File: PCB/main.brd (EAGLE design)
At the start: 100 x 100 mm, 81 parts, among them X1 BU-SMA-V

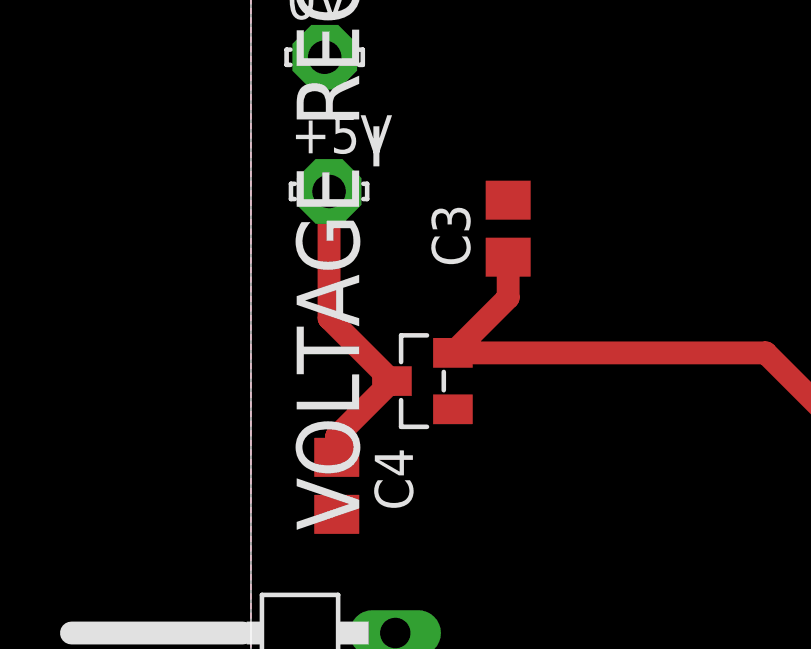
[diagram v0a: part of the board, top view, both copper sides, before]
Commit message: PCB Schematic Change
5V Supply Pad was not connected to 5V net
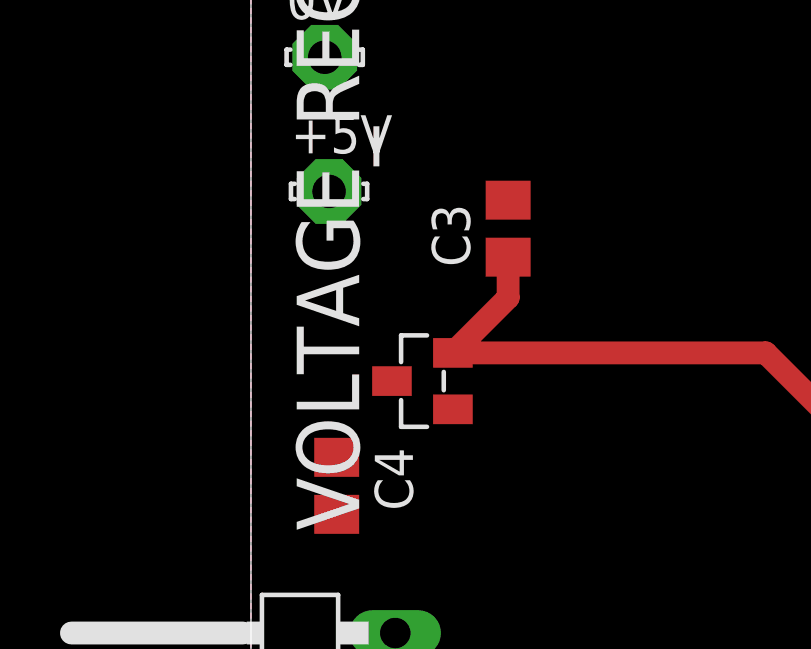
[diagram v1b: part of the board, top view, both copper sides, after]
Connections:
- removed net N$2: +5V.MP, C4.1, VOLTAGE_REGULATOR.3
- net +5V: now also +5V.MP, C4.1, VOLTAGE_REGULATOR.3
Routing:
- net N$2: track 10.5 -> 0.00 mm
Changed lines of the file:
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@@
 <wire x1="75.438" y1="73.152" x2="78.486" y2="76.2" width="0.3048" layer="1"/>
 <wire x1="78.486" y1="76.2" x2="80.4857" y2="76.2" width="0.3048" layer="1"/>
+<contactref element="C4" pad="1"/>
+<contactref element="+5V" pad="MP"/>
+<contactref element="VOLTAGE_REGULATOR" pad="3"/>
 <wire x1="31.75" y1="55.5625" x2="51.8175" y2="73.2325" width="0" layer="19" extent="1-1"/>
 <wire x1="29.21" y1="55.5625" x2="31.75" y2="55.5625" width="0" layer="19" extent="1-1"/>
 <wire x1="26.67" y1="55.5625" x2="29.21" y2="55.5625" width="0" layer="19" extent="1-1"/>
+<wire x1="4.699" y1="50.8" x2="26.67" y2="55.5625" width="0" layer="19" extent="1-1"/>
+<wire x1="2.8575" y1="48.2575" x2="4.699" y2="50.8" width="0" layer="19" extent="1-1"/>
+<wire x1="2.6025" y1="57.122" x2="4.699" y2="50.8" width="0" layer="19" extent="1-1"/>
 </signal>
 <signal name="BT-L">
@@
 <wire x1="49.2125" y1="68.3975" x2="49.3775" y2="68.2325" width="0.3048" layer="1"/>
 </signal>
-<signal name="N$2">
-<contactref element="VOLTAGE_REGULATOR" pad="3"/>
-<contactref element="C4" pad="1"/>
-<contactref element="+5V" pad="MP"/>
-<wire x1="4.699" y1="50.8" x2="2.6025" y2="52.8965" width="0.762" layer="1"/>
-<wire x1="2.6025" y1="52.8965" x2="2.6025" y2="57.122" width="0.762" layer="1"/>
-<wire x1="4.699" y1="50.8" x2="2.8575" y2="48.9585" width="0.762" layer="1"/>
-<wire x1="2.8575" y1="48.9585" x2="2.8575" y2="48.2575" width="0.762" layer="1"/>
-</signal>
 <signal name="N$10">

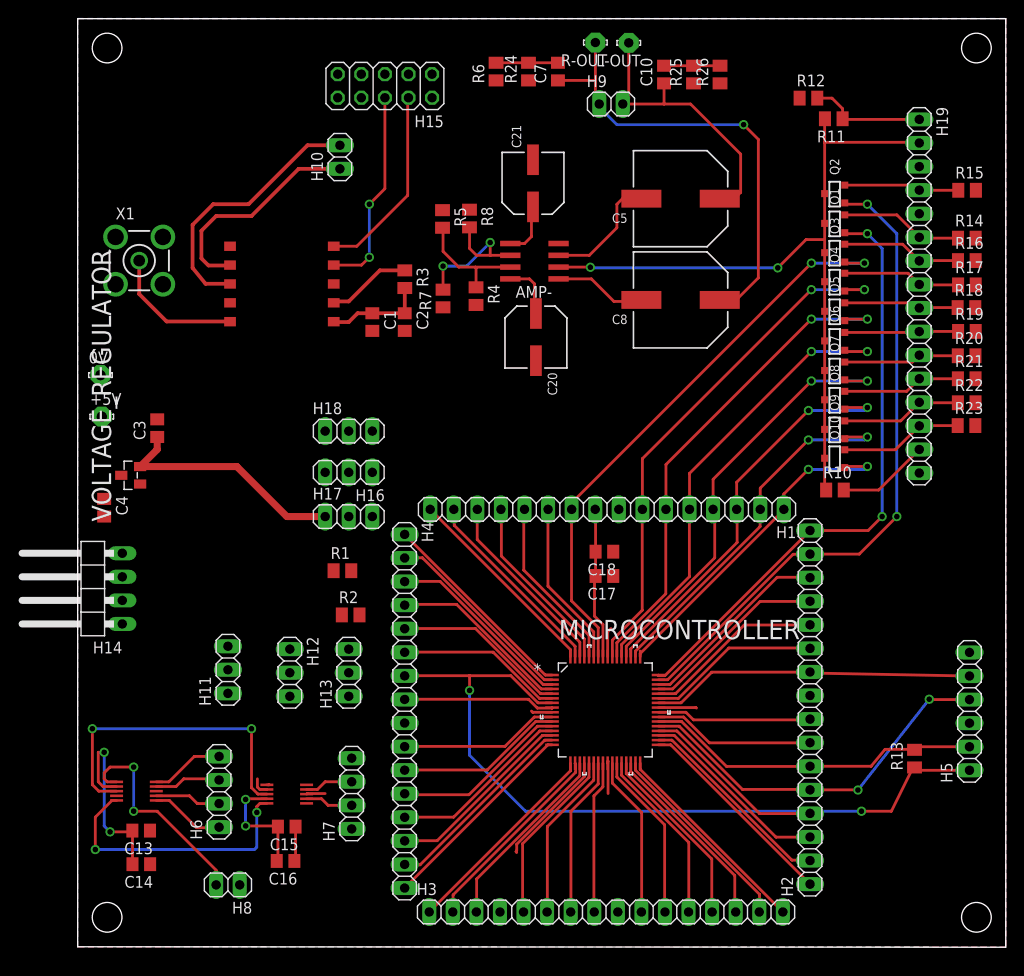
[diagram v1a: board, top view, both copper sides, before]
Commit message: PCB Layout
-All connections should be complete
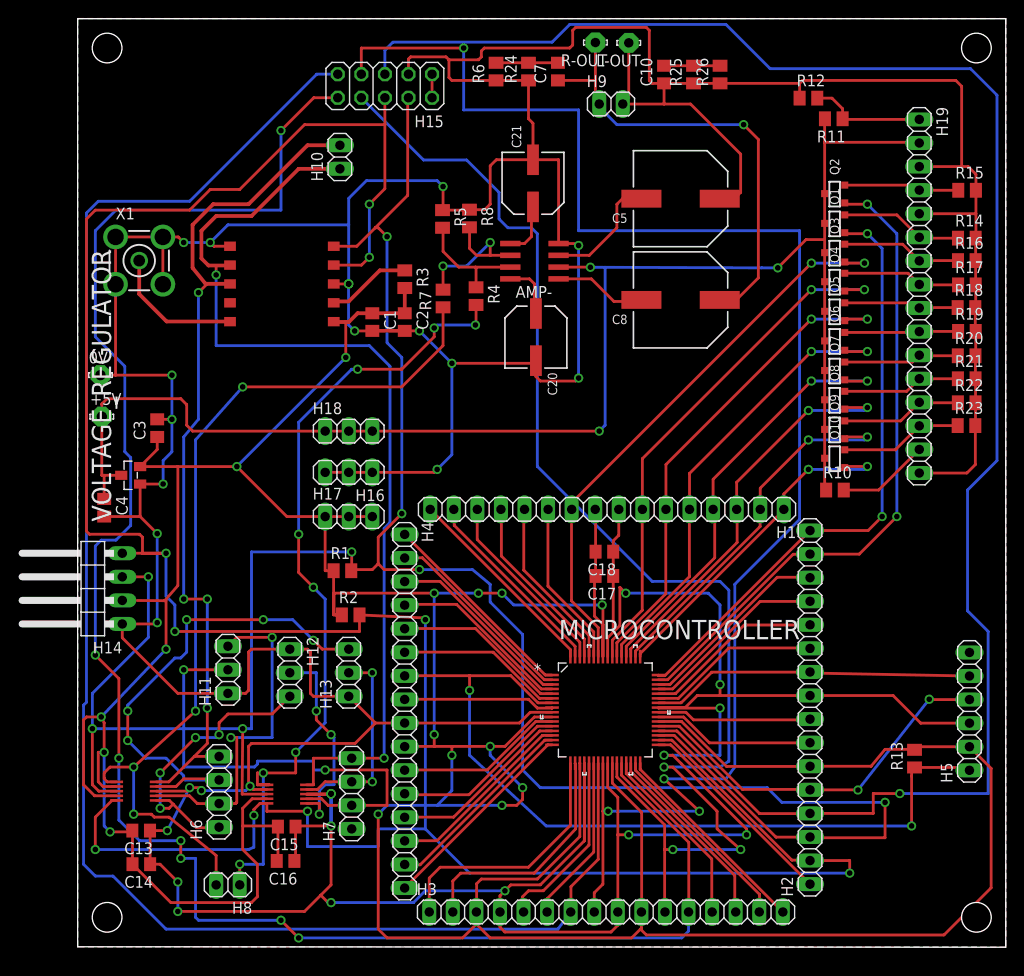
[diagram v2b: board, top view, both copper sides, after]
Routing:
- net GND: track 33.8 -> 734.7 mm, vias 0 -> 33
- net +3V3: track 179.1 -> 484.9 mm, vias 4 -> 16
- net SCL: track 73.4 -> 295.6 mm, vias 4 -> 9
- net SDA/MISO: track 76.0 -> 259.7 mm, vias 2 -> 8
- net XDCS: track 19.0 -> 198.6 mm, vias 0 -> 7
- net MOSI: track 20.0 -> 191.7 mm, vias 0 -> 1
- net XCS: track 17.3 -> 177.1 mm
- net DREQ: track 16.4 -> 170.7 mm, vias 0 -> 4
- net XRST: track 18.2 -> 142.9 mm, vias 0 -> 3
- net AMP-R: track 0.26 -> 89.0 mm, vias 0 -> 8
- net +5V: track 81.1 -> 167.8 mm, vias 2 -> 3
- net FM-R: track 24.1 -> 107.5 mm, vias 0 -> 2
- net AMP-L: track 23.4 -> 97.7 mm, vias 2 -> 4
- net FM-L: track 36.8 -> 94.3 mm, vias 0 -> 4
- net REC-L: track 7.16 -> 53.7 mm, vias 0 -> 5
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
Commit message: PCB Layout
- DRC performed (all clearance settings 6mil)
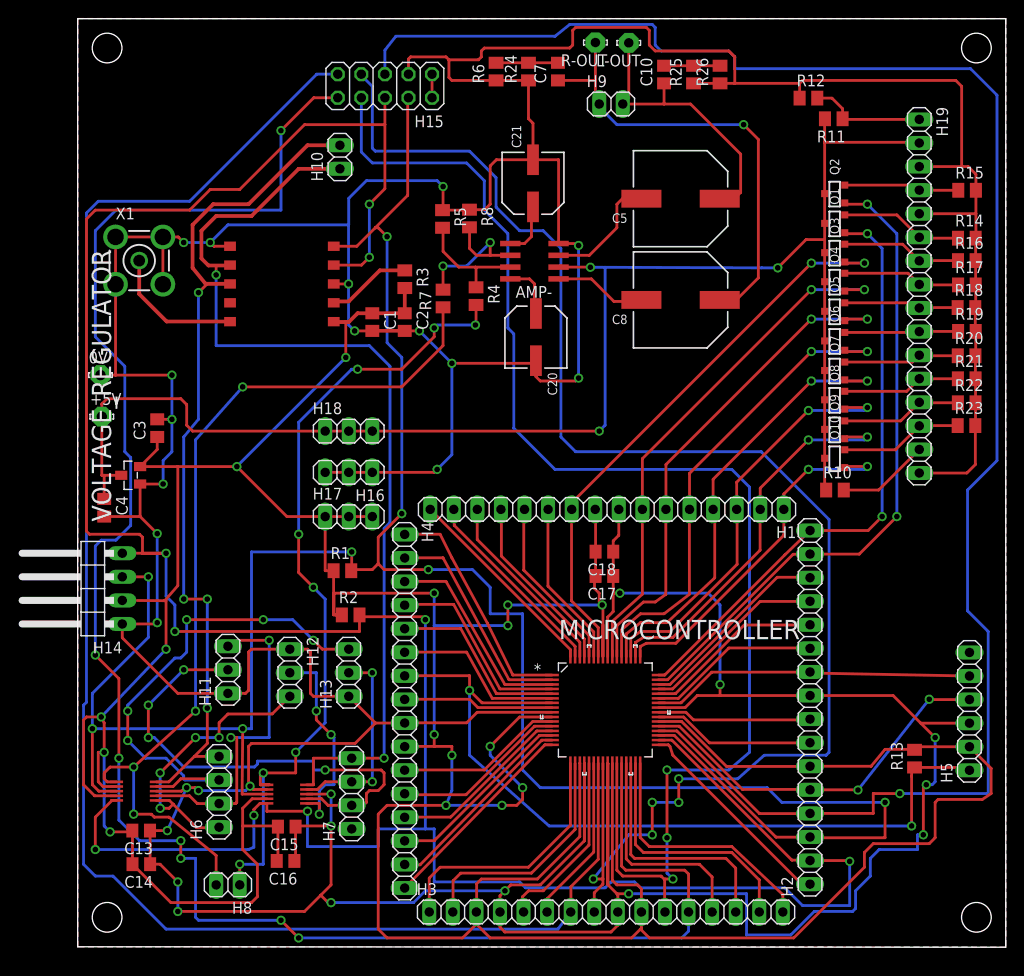
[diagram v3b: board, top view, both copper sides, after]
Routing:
- net GND: track 734.7 -> 754.7 mm, vias 33 -> 31
- net SCL: track 295.6 -> 304.9 mm
- net +3V3: track 484.9 -> 478.4 mm
- net PIC30: track 20.7 -> 26.5 mm
- net PIC31: track 21.6 -> 27.1 mm
- net PIC32: track 22.4 -> 27.7 mm
- net DREQ: track 170.7 -> 165.4 mm, vias 4 -> 5
- net XRST: track 142.9 -> 148.1 mm
- net PIC29: track 19.9 -> 24.1 mm
- net XDCS: track 198.6 -> 202.3 mm
- net PIC1: track 22.2 -> 25.1 mm
- net PIC2: track 21.3 -> 23.7 mm
- net D7-PIC: track 36.6 -> 38.6 mm
- net D6-PIC: track 40.0 -> 42.0 mm
- net D5-PIC: track 43.5 -> 45.5 mm
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
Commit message: PCB Layout
- Reworked the whole board to shrink it significantly
- Added DRC check file
- Fixed BT audio net name
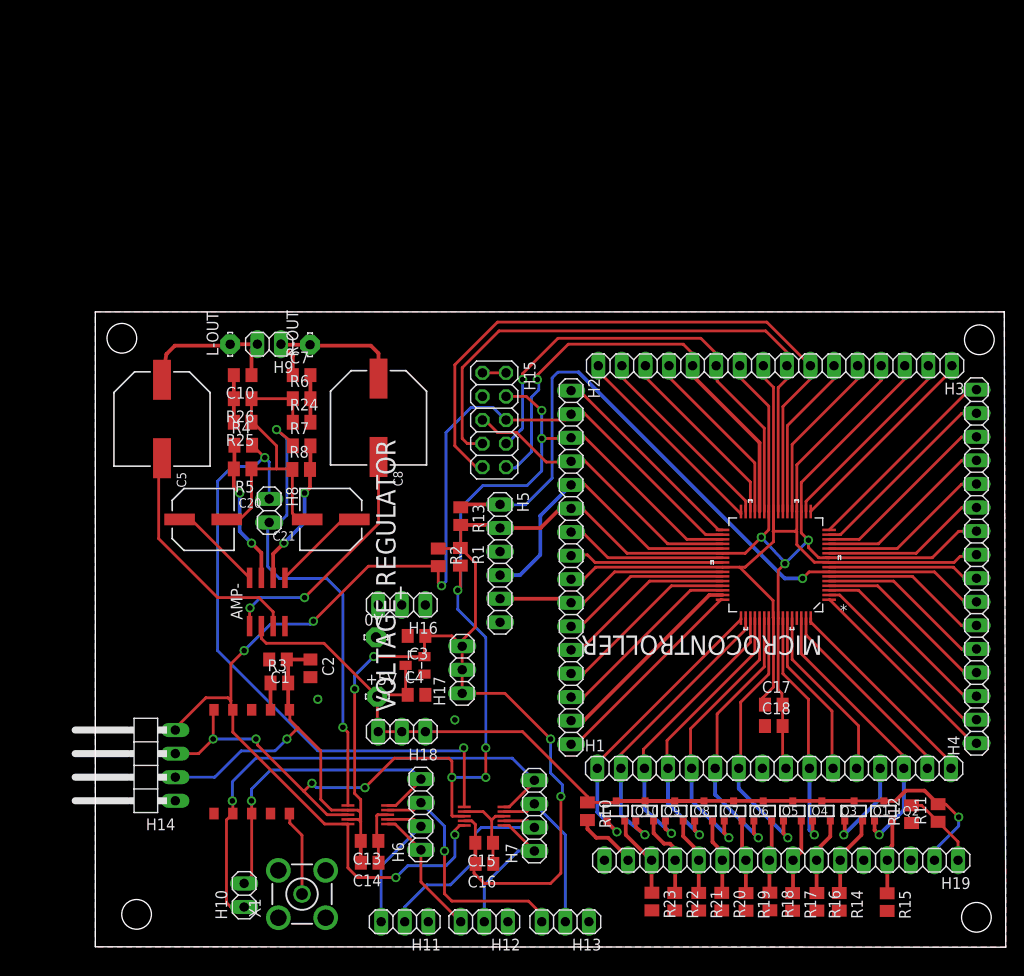
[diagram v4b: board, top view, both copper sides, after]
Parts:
- moved H10 80.2 mm to (17.9, 5.56)
- moved R12 77.9 mm to (89.9, 14.3), turned to 90 degrees
- moved R15 77.2 mm to (87.2, 4.81), turned to 270 degrees
- moved R11 75.6 mm to (92.7, 14.4), turned to 90 degrees
- moved U$2 74.8 mm to (23.3, -3.68), turned to 270 degrees
- moved R14 72.8 mm to (82.1, 4.84), turned to 270 degrees
- moved R16 71.0 mm to (79.7, 4.84), turned to 270 degrees
- moved X1 70.5 mm to (24.2, 5.68), turned to 90 degrees
- moved R17 69.1 mm to (77.0, 4.83), turned to 270 degrees
- moved R18 67.4 mm to (74.6, 4.88), turned to 270 degrees
- moved Q2 66.7 mm to (86.8, 14.7), turned to 0 degrees
- moved R19 65.9 mm to (72.0, 4.83), turned to 270 degrees
- moved R20 64.5 mm to (69.4, 4.86), turned to 270 degrees
- moved H4 63.6 mm to (96.8, 41.0), turned to 90 degrees
- moved R21 63.3 mm to (66.9, 4.85), turned to 270 degrees
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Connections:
- removed net BR-R: H7.1
- removed net PIC61: H1.13, MICROCONTROLLER.61
- removed net PIC62: H1.14, MICROCONTROLLER.62
- new net PIC47: H2.15, MICROCONTROLLER.47
- new net PIC48: H2.16, MICROCONTROLLER.48
- net BT-R: now also H7.1
- net E-PIC: now also H1.13; no longer H2.16, MICROCONTROLLER.48
- net RS-PIC: now also H1.14, MICROCONTROLLER.62; no longer H2.15, MICROCONTROLLER.47
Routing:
- net GND: track 754.7 -> 158.4 mm, vias 31 -> 2
- net +3V3: track 478.4 -> 274.6 mm, vias 16 -> 8
- net SCL: track 304.9 -> 136.2 mm, vias 9 -> 5
- net MOSI: track 193.6 -> 31.5 mm, vias 1 -> 0
- net XDCS: track 202.3 -> 51.7 mm, vias 7 -> 1
- net SDA/MISO: track 261.6 -> 134.1 mm, vias 8 -> 10
- net XCS: track 177.1 -> 71.9 mm
- net DREQ: track 165.4 -> 65.5 mm, vias 5 -> 0
- net XRST: track 148.1 -> 50.7 mm, vias 3 -> 1
- net FM-L: track 94.3 -> 34.9 mm, vias 4 -> 1
- net +5V: track 167.8 -> 110.1 mm, vias 3 -> 1
- net E-PIC: track 64.7 -> 10.3 mm, vias 2 -> 1
- net FM-R: track 107.5 -> 54.6 mm, vias 2 -> 1
- net AMP-L: track 97.7 -> 51.7 mm, vias 4 -> 2
- net RS-PIC: track 70.4 -> 30.7 mm, vias 2 -> 1
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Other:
- board size 100 x 100 mm -> 98.1 x 68.5 mm

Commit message: PCB Layout
-Track widths fixed
-Routing through headers neatened
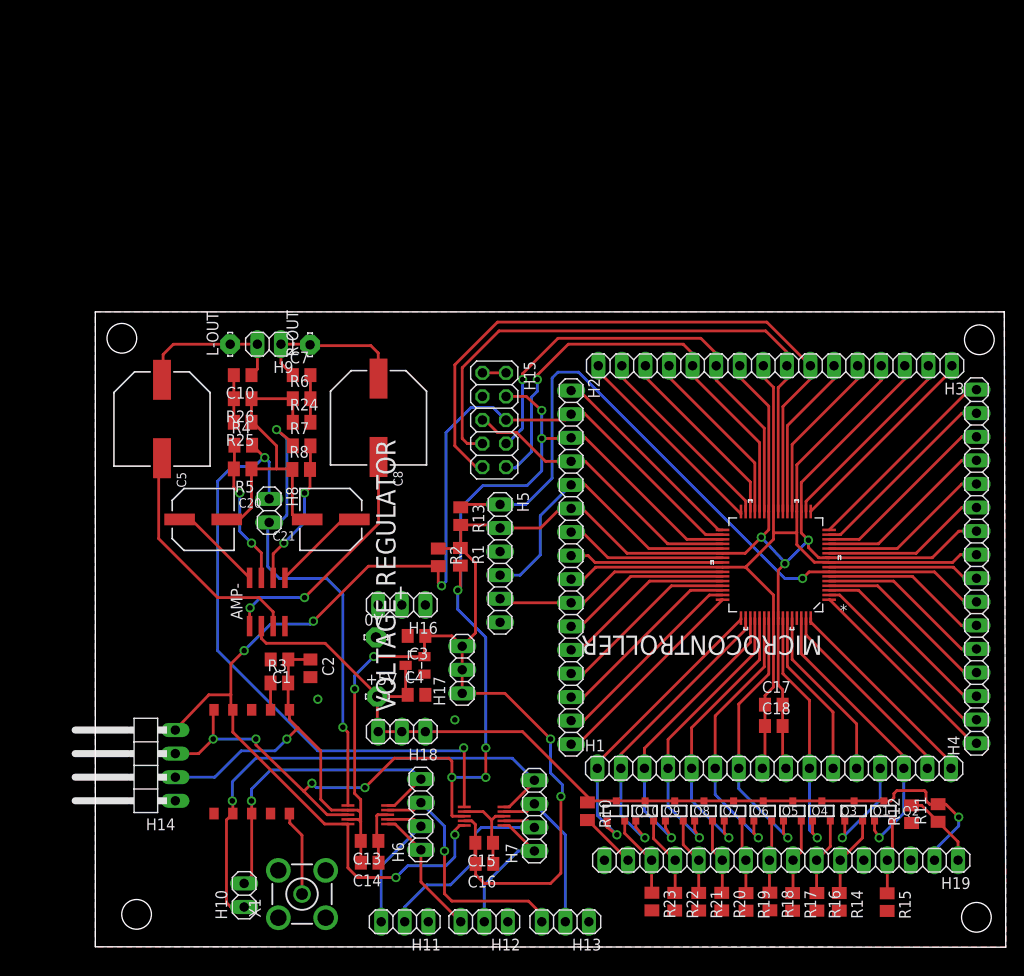
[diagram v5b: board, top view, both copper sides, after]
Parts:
- moved C1 0.16 mm to (21.7, 31.0)
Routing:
- net +5V: track 110.1 -> 101.2 mm
- net GND: track 158.4 -> 162.0 mm
- net XDCS: track 51.7 -> 50.6 mm
- net +3V3: track 274.6 -> 273.6 mm
- net PIC2: track 22.4 -> 21.4 mm
- net D0-PIC: track 26.3 -> 27.2 mm
- net E-PIC: track 10.3 -> 11.1 mm
- net PIC18: track 21.9 -> 21.2 mm
- net N$20: track 6.88 -> 6.17 mm
- net D7-PIC: track 31.9 -> 32.6 mm
- net D5-PIC: track 31.0 -> 31.6 mm
- net RS-PIC: track 30.7 -> 31.3 mm
- net SDA/MISO: track 134.1 -> 133.5 mm
